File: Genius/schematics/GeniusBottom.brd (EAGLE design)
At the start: 50 x 100 mm, 160 parts, among them IC1 TL074D, IC10 USBLC6-2SC6, IC2 IS42S16400J, IC3 LM321MF, IC4 CS4271, IC5 OPA1678IDR, IC6 OPA1678IDR, IC7 MIC2005A-1YM6, IC8 STM32H743ZGTx, IC9 N25Q128A13, Q1 SI2309CDS, Q2 2N7002P, Q601 BC846, Q701 BC846, Q801 BC846, Q903 BC846, U4 TLV1117LV33, X1 53048-05, X4 FH12-24S-0.5SH, Y1 24.576MHz, Y2 25MHz

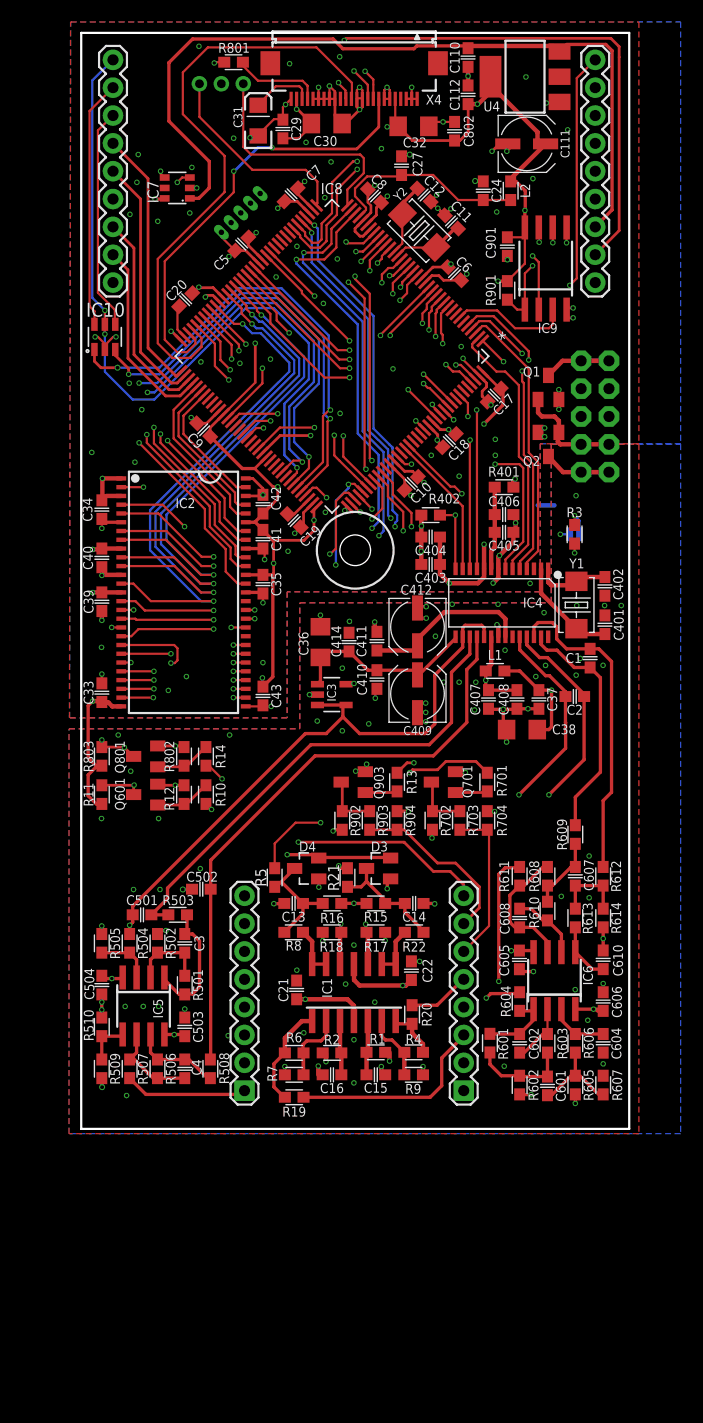
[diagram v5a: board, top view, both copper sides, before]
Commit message: Renumbered parts. Rev02.
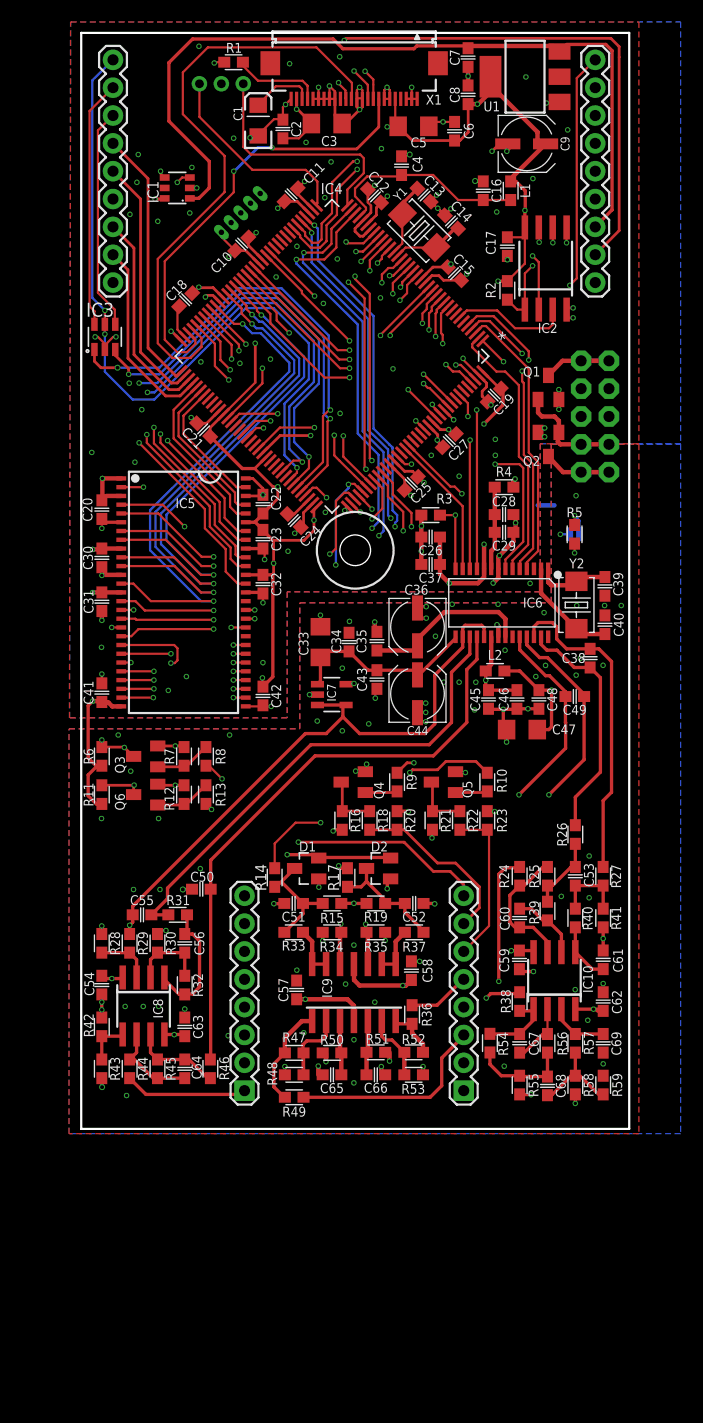
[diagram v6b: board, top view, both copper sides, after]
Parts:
- removed C110, C112, C405, C410, C411, C414, C802, C901: 100n, Rebel:C0603
- removed C111, C412: 47u, Rebel:CPOL-5
- removed C401, C402: 39p C0G, Rebel:C0603
- removed C403: 1u, Rebel:C0603
- removed R401: 5R1, Rebel:0603
- removed R402, R803, R901, R904: 10k, Rebel:0603
- removed R701: 1k, Rebel:0603
- removed R702, R902: 2k, Rebel:0603
- removed R703, R903: 100R, Rebel:0603
- removed R801: 560k, Rebel:0603
- removed R802: 1M, Rebel:0603
- removed X4: FH12-24S-0.5SH, con-hirose:FH12-24S-0.5SH
- added C23, C25, C48, C57, C58: 100n, Rebel:C0603
- added C47: 10u, Rebel:C1206
- added C49: 47n, Rebel:C0603
- added C51, C52, C65, C66: 10n C0G, Rebel:C0603
- added C56, C64: 100p C0G, Rebel:C0603
- added R33, R37, R50, R51: 2k, Rebel:0603
- added R34, R35: 100k, Rebel:0603
- added R36, R49: 100R, Rebel:0603
- added R47, R52: 20k, Rebel:0603
- added R48, R53: 10k, Rebel:0603
- added X100: 53048-05, con-molex:53048-05
- C1: value 47n -> 4u7 16V Tantalum; device Rebel:C0603 -> smartplug:EIA3216
- C11, C12: value 20p -> 100n
- C13, C14: value 10n C0G -> 20p
- C15, C16: value 10n C0G -> 100n
- C18: value 1u -> 4u7
- C19, C20: value 4u7 -> 100n
- C2: value 47n -> 100n
- C24: value 100n -> 4u7
- C27: value 10n -> 1u
- C3: value 100p C0G -> 10u; device Rebel:C0603 -> Rebel:C1206
- C30, C32: value 10u -> 100n; device Rebel:C1206 -> Rebel:C0603
- C31: value 4u7 16V Tantalum -> 100n; device smartplug:EIA3216 -> Rebel:C0603
- C33, C5: value 100n -> 10u; device Rebel:C0603 -> Rebel:C1206
- C36: value 10u -> 47u; device Rebel:C1206 -> Rebel:CPOL-5
- C37: value 100n -> 1u
- C38: value 10u -> 47n; device Rebel:C1206 -> Rebel:C0603
- C39, C40: value 100n -> 39p C0G
- C4: value 100p C0G -> 10n
- C9: value 100n -> 47u; device Rebel:C0603 -> Rebel:CPOL-5
- IC1: value TL074D -> MIC2005A-1YM6; device linear:SO14 -> James:SOT23-6
- IC10: value USBLC6-2SC6 -> OPA1678IDR; device usblc6:SOT-23-6L -> linear:SO08
- IC2: value IS42S16400J -> N25Q128A13; device James:TSOP54-400 -> Rebel:SO8W
- IC3: value LM321MF -> USBLC6-2SC6; device linear:SOT23-5 -> usblc6:SOT-23-6L
- IC4: value CS4271 -> STM32H743ZGTx; device Rebel:TSSOP28-0.65-9.7X4.4MM -> Rebel:QFP50P2200X2200X160-144N
- IC5: value OPA1678IDR -> IS42S16400J; device linear:SO08 -> James:TSOP54-400
- IC6: value OPA1678IDR -> CS4271; device linear:SO08 -> Rebel:TSSOP28-0.65-9.7X4.4MM
- IC7: value MIC2005A-1YM6 -> LM321MF; device James:SOT23-6 -> linear:SOT23-5
- IC8: value STM32H743ZGTx -> OPA1678IDR; device Rebel:QFP50P2200X2200X160-144N -> linear:SO08
- IC9: value N25Q128A13 -> TL074D; device Rebel:SO8W -> linear:SO14
- JP1: value (none) -> M09; device SparkFun:1X08 -> SparkFun:1X09
- JP4: value M09 -> (none); device SparkFun:1X09 -> SparkFun:1X08
- R1: value 2k -> 560k
- R10: value 100k -> 1k
- R13: value 1k -> 100k
- R14, R17, R18: value 100k -> 100R
- R16: value 1k -> 2k
- R19: value 100R -> 1k
- R2: value 2k -> 10k
- R20, R5: value 100R -> 10k
- R21: value 100R -> 2k
- R22: value 2k -> 100R
- R4: value 20k -> 5R1
- R6: value 20k -> 10k
- R7: value 10k -> 1M
- R8: value 2k -> 100k
- R9: value 10k -> 1k
- X1: value 53048-05 -> FH12-24S-0.5SH; device con-molex:53048-05 -> con-hirose:FH12-24S-0.5SH
- Y1: value 24.576MHz -> 25MHz
- Y2: value 25MHz -> 24.576MHz
- moved JP1 94.8 mm to (2.90, 97.5), turned to 270 degrees
- moved JP4 94.8 mm to (34.9, 3.49), turned to 90 degrees
- moved R1 91.3 mm to (13.9, 97.3), turned to 0 degrees
- moved C4 84.7 mm to (29.2, 87.9)
- moved C16 81.8 mm to (36.7, 85.6), turned to 90 degrees
- moved C3 75.9 mm to (22.4, 91.7), turned to 180 degrees
- moved IC1 75.2 mm to (8.76, 85.9), turned to 90 degrees
- moved C15 73.4 mm to (34.1, 78.0), turned to 315 degrees
- moved IC10 71.6 mm to (43.2, 13.5)
- moved R2 71.4 mm to (38.9, 76.5), turned to 270 degrees
- moved IC9 68.3 mm to (24.9, 12.4)
- moved C13 65.7 mm to (31.3, 85.2), turned to 315 degrees
- moved C14 62.3 mm to (33.8, 82.8), turned to 135 degrees
- moved IC8 61.7 mm to (5.69, 11.2), turned to 180 degrees
- moved C2 58.2 mm to (18.4, 91.2), turned to 270 degrees
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- renumbered C404 to C26, C406 to C28, C407 to C45, C408 to C46, C409 to C44, C501 to C55, C502 to C50, C503 to C63, C504 to C54, C601 to C68, C602 to C67, C604 to C69, C605 to C59, C606 to C62, C607 to C53, C608 to C60, C610 to C61, D3 to D2, D4 to D1, Q601 to Q6, Q701 to Q5, Q801 to Q3, Q903 to Q4, R501 to R32, R502 to R30, R503 to R31, R504 to R29, R505 to R28, R506 to R45, R507 to R44, R508 to R46, R509 to R43, R510 to R42, R601 to R54, R602 to R55, R603 to R56, R604 to R38, R605 to R58, R606 to R57, R607 to R59, R608 to R25, R609 to R26, R610 to R39, R611 to R24, R612 to R27, R613 to R40, R614 to R41, R704 to R23, U4 to U1
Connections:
- net +12V: now also C2.2, C3.2, C57.1, IC10.8, IC7.5, IC8.8, IC9.4, JP2.8, R16.1, R21.2, X1.23; no longer C21.1, C29.2, C30.2, IC1.4, IC3.5, IC5.8, IC6.8, JP4.8, R702.2, R902.1, X4.23
- net +3.3V: now also C11.1, C12.1, C15.1, C19.1, C20.1, C21.1, C22.1, C23.1, C25.1, C27.1, C30.1, C31.1, C32.1, C37.1, C5.2, C6.2, C9.+, IC2.8, IC4.108, IC4.121, IC4.131, IC4.144, IC4.17, IC4.30, IC4.32, IC4.39, IC4.52, IC4.62, IC4.72, IC4.84, IC4.95, IC5.1, IC5.14, IC5.27, IC5.3, IC5.43, IC5.49, IC5.9, IC6.10, L1.2, R2.1, R6.1, X1.5, X100.1; no longer C111.+, C112.1, C18.1, C32.2, C33.1, C34.1, C35.1, C39.1, C40.1, C403.1, C43.1, C5.1, C6.1, C7.1, C802.2, C9.1, C901.1, IC2.1, IC2.14, IC2.27, IC2.3, IC2.43, IC2.49, IC2.9, IC4.10, IC8.108, IC8.121, IC8.131, IC8.144, IC8.17, IC8.30, IC8.32, IC8.39, IC8.52, IC8.62, IC8.72, IC8.84, IC8.95, IC9.8, L2.2, R803.1, R901.1, X1.1, X4.5
- net +5V: now also C47.1, C48.1, C7.2, IC1.1, JP2.7, L2.1, R4.2; no longer C110.2, C37.1, C38.1, IC7.1, JP4.7, L1.1, R401.2
- net -12V: now also C58.1, IC10.4, IC7.2, IC8.4, IC9.11; no longer C22.1, IC1.11, IC3.2, IC5.4, IC6.4
- net ADC0: now also IC4.34, R14.2; no longer IC8.34, R5.2
- net ADC1: now also IC4.35, R17.2; no longer IC8.35, R21.2
- net AINA: now also IC6.17; no longer IC4.17
- net AINB: now also IC6.18; no longer IC4.18
- net ANALOG_OUTA: now also IC10.1; no longer IC6.1
- net ANALOG_OUTB: now also IC10.7; no longer IC6.7
- net AOUTA+: now also C49.1, IC6.25; no longer C2.1, IC4.25
- net AOUTA-: now also C49.2, IC6.24; no longer C2.2, IC4.24
- net AOUTB+: now also C38.2, IC6.26; no longer C1.2, IC4.26
- net AOUTB-: now also C38.1, IC6.27; no longer C1.1, IC4.27
- net BOOT: now also IC4.138, R5.2; no longer IC8.138, R3.2
- net CS_!CS: now also IC4.124, IC6.13; no longer IC4.13, IC8.124
- net CS_!RST: now also IC4.125, IC6.14, R3.2; no longer IC4.14, IC8.125, R402.2
- net CS_LRCK: now also IC4.3, IC6.4; no longer IC4.4, IC8.3
- net CS_SCK: now also IC4.1, IC6.11; no longer IC4.11, IC8.1
- net CS_SCLK: now also IC4.4, IC6.5; no longer IC4.5, IC8.4
- net CS_SDA: now also IC4.5, IC6.12; no longer IC4.12, IC8.5
- net CS_SDIN: now also IC4.122, IC6.7; no longer IC4.7, IC8.122
- net CS_SDOUT: now also IC4.2, IC6.6; no longer IC4.6, IC8.2
- net CS_VQ1: now also C33.2, C34.1, C43.1, IC6.15, IC7.1; no longer C36.2, C410.1, C414.1, IC3.1, IC4.15
- net CS_VREF: now also IC6.16, IC6.19, IC7.3, IC7.4; no longer IC3.3, IC3.4, IC4.16, IC4.19
- net CVINA: now also IC9.12, JP3.5, R34.2; no longer IC1.12, JP1.5, R18.2
- net CVINB: now also IC9.10, JP3.3, R35.2; no longer IC1.10, JP1.3, R17.2
- net CVOUTA: now also JP4.5, R36.2; no longer JP3.5, R20.2
- net CVOUTB: now also JP4.3, R49.2; no longer JP3.3, R19.2
- net DAC1: now also IC4.40, R51.1; no longer IC8.40, R1.1
- net DAC2: now also IC4.41, R50.1; no longer IC8.41, R2.1
- net DRAM_!CAS: now also IC4.132, IC5.17; no longer IC2.17, IC8.132
- net DRAM_!CS: now also IC4.136, IC5.19; no longer IC2.19, IC8.136
- net DRAM_!RAS: now also IC4.49, IC5.18; no longer IC2.18, IC8.49
- net DRAM_!WE: now also IC4.26, IC5.16; no longer IC2.16, IC8.26
- net DRAM_A0: now also IC4.10, IC5.23; no longer IC2.23, IC8.10
- net DRAM_A1: now also IC4.11, IC5.24; no longer IC2.24, IC8.11
- net DRAM_A10: now also IC4.56, IC5.22; no longer IC2.22, IC8.56
- net DRAM_A11: now also IC4.57, IC5.35; no longer IC2.35, IC8.57
- net DRAM_A2: now also IC4.12, IC5.25; no longer IC2.25, IC8.12
- net DRAM_A3: now also IC4.13, IC5.26; no longer IC2.26, IC8.13
- net DRAM_A4: now also IC4.14, IC5.29; no longer IC2.29, IC8.14
- net DRAM_A5: now also IC4.15, IC5.30; no longer IC2.30, IC8.15
- net DRAM_A6: now also IC4.50, IC5.31; no longer IC2.31, IC8.50
- net DRAM_A7: now also IC4.53, IC5.32; no longer IC2.32, IC8.53
- net DRAM_A8: now also IC4.54, IC5.33; no longer IC2.33, IC8.54
- net DRAM_A9: now also IC4.55, IC5.34; no longer IC2.34, IC8.55
- net DRAM_BA0: now also IC4.89, IC5.20; no longer IC2.20, IC8.89
- net DRAM_BA1: now also IC4.90, IC5.21; no longer IC2.21, IC8.90
- net DRAM_CKE: now also IC4.135, IC5.37; no longer IC2.37, IC8.135
- net DRAM_CLK: now also IC4.93, IC5.38; no longer IC2.38, IC8.93
- net DRAM_DQ0: now also IC4.85, IC5.2; no longer IC2.2, IC8.85
- net DRAM_DQ1: now also IC4.86, IC5.4; no longer IC2.4, IC8.86
- net DRAM_DQ10: now also IC4.66, IC5.45; no longer IC2.45, IC8.66
- net DRAM_DQ11: now also IC4.67, IC5.47; no longer IC2.47, IC8.67
- net DRAM_DQ12: now also IC4.68, IC5.48; no longer IC2.48, IC8.68
- net DRAM_DQ13: now also IC4.77, IC5.50; no longer IC2.50, IC8.77
- net DRAM_DQ14: now also IC4.78, IC5.51; no longer IC2.51, IC8.78
- net DRAM_DQ15: now also IC4.79, IC5.53; no longer IC2.53, IC8.79
- net DRAM_DQ2: now also IC4.114, IC5.5; no longer IC2.5, IC8.114
- net DRAM_DQ3: now also IC4.115, IC5.7; no longer IC2.7, IC8.115
- net DRAM_DQ4: now also IC4.58, IC5.8; no longer IC2.8, IC8.58
- net DRAM_DQ5: now also IC4.59, IC5.10; no longer IC2.10, IC8.59
- net DRAM_DQ6: now also IC4.60, IC5.11; no longer IC2.11, IC8.60
- net DRAM_DQ7: now also IC4.63, IC5.13; no longer IC2.13, IC8.63
- net DRAM_DQ8: now also IC4.64, IC5.42; no longer IC2.42, IC8.64
- net DRAM_DQ9: now also IC4.65, IC5.44; no longer IC2.44, IC8.65
- net DRAM_LDQM: now also IC4.141, IC5.15; no longer IC2.15, IC8.141
- net DRAM_UDQM: now also IC4.142, IC5.39; no longer IC2.39, IC8.142
- net ENC1_A: now also IC4.42, JP2.2; no longer IC8.42, JP4.2
- net ENC1_B: now also IC4.43, JP2.3; no longer IC8.43, JP4.3
- net ENC1_SW: now also IC4.129, JP2.1; no longer IC8.129, JP4.1
- net ENC2_A: now also IC4.110, JP2.5; no longer IC8.110, JP4.5
- net ENC2_B: now also IC4.133, JP2.6; no longer IC8.133, JP4.6
- net ENC2_SW: now also IC4.134, JP2.4; no longer IC8.134, JP4.4
- net FLASH_CLK: now also IC2.6, IC4.19; no longer IC8.19, IC9.6
- net FLASH_HOLD: now also IC2.7, IC4.22; no longer IC8.22, IC9.7
- net FLASH_MISO: now also IC2.2, IC4.20; no longer IC8.20, IC9.2
- net FLASH_MOSI: now also IC2.5, IC4.21; no longer IC8.21, IC9.5
- net FLASH_NCS: now also IC2.1, IC4.18, R2.2; no longer IC8.18, IC9.1, R901.2
- net FLASH_W: now also IC2.3, IC4.7; no longer IC8.7, IC9.3
- net GND: now also C1.C, C2.1, C23.2, C25.2, C29.2, C3.1, C30.2, C31.2, C32.2, C33.1, C36.-, C4.2, C47.2, C48.2, C5.1, C51.2, C52.2, C57.2, C58.2, C6.1, C65.2, C66.2, C7.1, C9.-, IC1.2, IC2.4, IC3.2, IC4.107, IC4.120, IC4.130, IC4.143, IC4.16, IC4.31, IC4.38, IC4.51, IC4.61, IC4.83, IC4.94, IC5.12, IC5.28, IC5.41, IC5.46, IC5.52, IC5.54, IC5.6, IC6.21, IC6.8, JP1.9, JP4.4, R1.1, R19.2, R20.1, R34.1, R35.1, R48.1, R5.1, R53.1, R7.2, X1.1, X1.11, X1.12, X1.16, X1.17, X1.18, X1.19, X1.2, X1.20, X1.24, X1.6, X1.7, X100.3; no longer C110.1, C111.-, C112.2, C29.1, C30.1, C31.C, C32.1, C33.2, C36.1, C38.2, C401.2, C402.2, C403.2, C405.2, C410.2, C411.2, C412.-, C414.2, C5.2, C6.2, C7.2, C802.1, C9.2, C901.2, IC10.2, IC2.12, IC2.28, IC2.41, IC2.46, IC2.52, IC2.54, IC2.6, IC4.21, IC4.8, IC7.2, IC8.107, IC8.120, IC8.130, IC8.143, IC8.16, IC8.31, IC8.38, IC8.51, IC8.61, IC8.83, IC8.94, IC9.4, JP1.4, JP4.9, R16.2, R17.1, R18.1, R402.1, R7.1, R801.1, R802.2, R9.1, R904.1, X4.1, X4.11, X4.12, X4.16, X4.17, X4.18, X4.19, X4.2, X4.20, X4.24, X4.3, X4.6, X4.7
- net INL: now also JP3.2; no longer JP1.2
- net INR: now also JP3.1; no longer JP1.1
- net N$11: now also C13.1, IC4.24, Y1.1; no longer C12.1, IC8.24, Y2.1
- net N$12: now also IC9.2, R47.1, R48.2; no longer IC1.2, R6.1, R7.2
- net N$13: now also IC10.2; no longer IC6.2
- net N$14: now also IC10.3; no longer IC6.3
- net N$15: now also IC9.6, R52.1, R53.2; no longer IC1.6, R4.1, R9.2
- net N$17: now also C14.1, IC4.23, Y1.2; no longer C11.1, IC8.23, Y2.2
- net N$18: now also C39.1, IC6.1, Y2.1; no longer C402.1, IC4.1, Y1.1
- net N$19: now also IC3.6, JP1.2; no longer IC10.6, JP2.2
- net N$2: now also C51.1, R14.1, R15.1, R33.2; no longer C13.1, R16.1, R5.1, R8.2
- net N$20: now also C35.1, C36.+, IC6.22; no longer C411.1, C412.+, IC4.22
- net N$21: now also C40.1, IC6.2, Y2.2; no longer C401.1, IC4.2, Y1.2
- net N$22: now also C52.1, R17.1, R19.1, R37.2; no longer C14.1, R15.1, R21.1, R22.2
- net N$27: now also IC10.6; no longer IC6.6
- net N$28: now also IC10.5; no longer IC6.5
- net N$3: now also IC6.20, L2.2; no longer IC4.20, L1.2
- net N$30: now also IC9.13, IC9.14, R33.1; no longer IC1.13, IC1.14, R8.1
- net N$31: now also C65.1, IC9.3, R50.2; no longer C16.1, IC1.3, R2.2
- net N$32: now also IC9.1, R47.2, R49.1; no longer IC1.1, R19.1, R6.2
- net N$33: now also C24.1, IC4.106; no longer C19.1, IC8.106
- net N$34: now also C18.1, IC4.71; no longer C20.1, IC8.71
- net N$36: now also IC8.3; no longer IC5.3
- net N$37: now also R13.2; no longer R10.2
- net N$38: now also C56.1, IC8.2; no longer C3.1, IC5.2
- net N$39: now also R10.1; no longer R701.1
- net N$4: now also IC9.7, R36.1, R52.2; no longer IC1.7, R20.1, R4.2
- net N$40: now also C56.2, IC8.1; no longer C3.2, IC5.1
- net N$41: now also R21.1, R22.1; no longer R702.1, R703.1
- net N$42: now also IC8.5; no longer IC5.5
- net N$43: now also C64.1, IC8.6; no longer C4.1, IC5.6
- net N$44: now also C66.1, IC9.5, R51.2; no longer C15.1, IC1.5, R1.2
- net N$45: now also C64.2, IC8.7; no longer C4.2, IC5.7
- net N$46: now also IC4.48; no longer IC8.48
- net N$47: now also R9.1; no longer R13.1
- net N$48: now also IC4.100; no longer IC8.100
- net N$5: now also IC9.8, IC9.9, R37.1; no longer IC1.8, IC1.9, R22.1
- net N$51: now also R16.2, R18.1; no longer R902.2, R903.1
- net N$54: now also R7.1, R8.2; no longer R14.2, R802.1
- net N$55: now also IC3.4, JP1.3; no longer IC10.4, JP2.3
- net N$6: now also C1.A, X1.22; no longer C31.A, X4.22
- net N$8: now also R1.2, X1.21; no longer R801.2, X4.21
- net NRST: now also IC4.25, X100.5; no longer IC8.25, X1.5
- net OLED_CS: now also IC4.70, X1.8; no longer IC8.70, X4.8
- net OLED_DC: now also IC4.29, X1.10; no longer IC8.29, X4.10
- net OLED_MOSI: now also IC4.27, X1.14; no longer IC8.27, X4.14
- net OLED_RST: now also IC4.28, X1.9; no longer IC8.28, X4.9
- net OLED_SCK: now also IC4.69, X1.13; no longer IC8.69, X4.13
- net OUTL: now also JP4.2; no longer JP3.2
- net OUTR: now also JP4.1; no longer JP3.1
- net SWCLK: now also IC4.109, X100.2; no longer IC8.109, X1.2
- net SWDIO: now also IC4.105, X100.4; no longer IC8.105, X1.4
- net SW_A: now also IC4.111, JP3.8; no longer IC8.111, JP1.8
- net SW_B: now also IC4.113, JP4.8; no longer IC8.113, JP3.8
- net TRINA: now also JP3.7, R8.1; no longer JP1.7, R14.1
- net TRINB: now also JP3.6, R13.1; no longer JP1.6, R10.1
- net TROUTA: now also JP4.7, R18.2, R20.2; no longer JP3.7, R903.2, R904.2
- net TROUTB: now also JP4.6, R22.2; no longer JP3.6, R703.2
- net TR_IN_A: now also IC4.112, R6.2; no longer IC8.112, R803.2
- net TR_IN_B: now also IC4.116; no longer IC8.116
- net TR_OUT_A: now also IC4.118, R9.2; no longer IC8.118, R13.2
- net TR_OUT_B: now also IC4.117, R10.2; no longer IC8.117, R701.2
- net UART5_RX: now also IC4.73, JP1.4; no longer IC8.73, JP2.4
- net UART5_TX: now also IC4.74, JP1.5; no longer IC8.74, JP2.5
- net UART_MCU_RX: now also IC4.37; no longer IC8.37
- net UART_MCU_TX: now also IC4.36; no longer IC8.36
- net USBD_DM: now also IC3.1, IC4.103; no longer IC10.1, IC8.103
- net USBD_DP: now also IC3.3, IC4.104; no longer IC10.3, IC8.104
- net USBD_VBUS: now also IC3.5, IC4.101, JP1.1; no longer IC10.5, IC8.101, JP2.1
- net USBH_DM: now also IC4.75, JP1.7; no longer IC8.75, JP2.7
- net USBH_DP: now also IC4.76, JP1.8; no longer IC8.76, JP2.8
- net USBH_PWR_EN: now also IC1.3, IC4.99; no longer IC7.3, IC8.99
- net USBH_PWR_FAULT: now also IC1.4, IC4.102; no longer IC7.4, IC8.102
- net USBH_VBUS: now also IC1.6, JP1.6; no longer IC7.6, JP2.6
- net VD: now also C29.1, IC6.9, R4.1; no longer C405.1, IC4.9, R401.1
- net VDDA: now also C16.1, C4.1, IC4.33, L1.1; no longer C24.1, C27.1, IC8.33, L2.1
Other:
- board text added: "Genius Rev02"
- board text removed: "Genius Rev01"

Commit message: added I2C bus
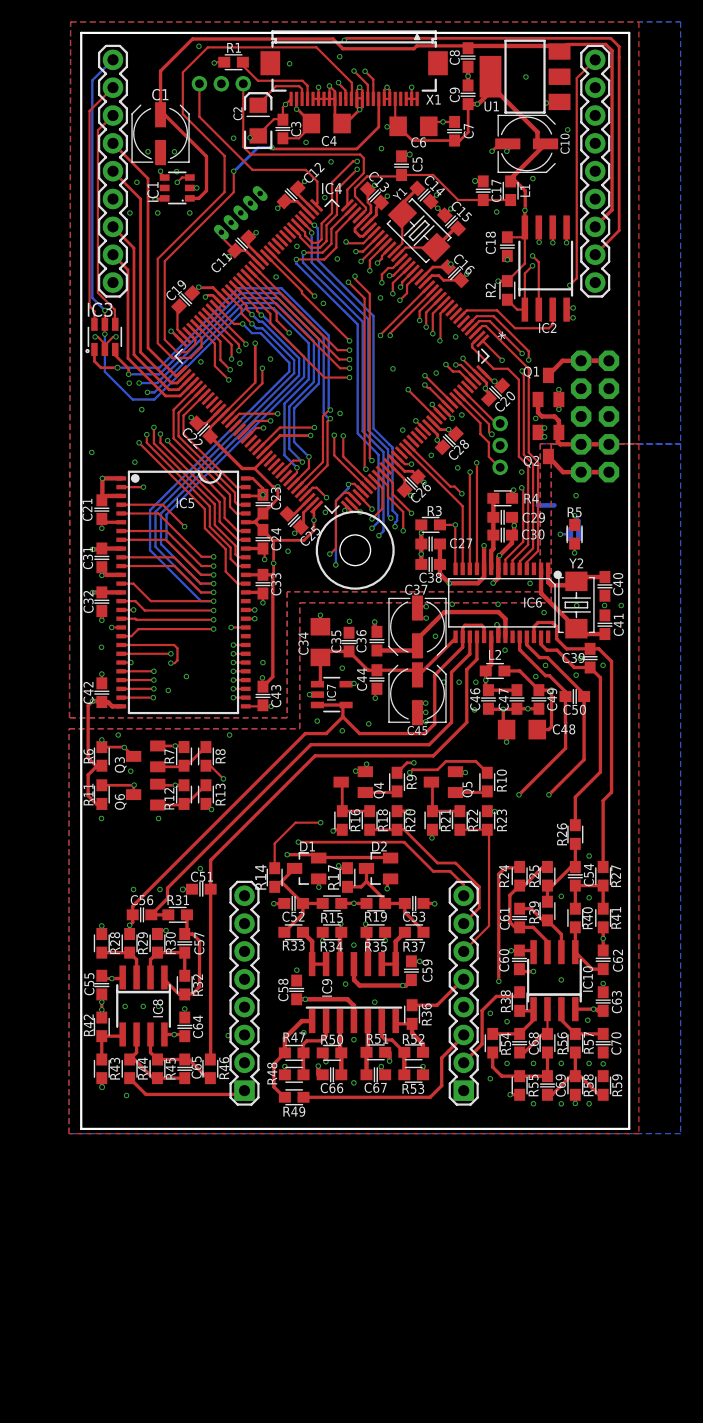
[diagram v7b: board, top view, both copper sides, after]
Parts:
- added C70: 100p C0G, Rebel:C0603
- added I2C: (no value), Rebel:JST-B3B-PH-KL
- C1: value 4u7 16V Tantalum -> 47u; device smartplug:EIA3216 -> Rebel:CPOL-5
- C10: value 100n -> 47u; device Rebel:C0603 -> Rebel:CPOL-5
- C13: value 20p -> 100n
- C15: value 100n -> 20p
- C18, C24: value 4u7 -> 100n
- C19, C25: value 100n -> 4u7
- C2: value 100n -> 4u7 16V Tantalum; device Rebel:C0603 -> smartplug:EIA3216
- C27: value 1u -> 100n
- C29, C46: value 100n -> 1u
- C3, C33, C47: value 10u -> 100n; device Rebel:C1206 -> Rebel:C0603
- C34, C48, C6: value 100n -> 10u; device Rebel:C0603 -> Rebel:C1206
- C36, C9: value 47u -> 100n; device Rebel:CPOL-5 -> Rebel:C0603
- C37: value 1u -> 47u; device Rebel:C0603 -> Rebel:CPOL-5
- C38: value 47n -> 1u
- C39: value 39p C0G -> 47n
- C4: value 10n -> 10u; device Rebel:C0603 -> Rebel:C1206
- C41: value 100n -> 39p C0G
- C44: value 10u -> 100n; device Rebel:CPOL-5 -> Rebel:C0603
- C45: value 1u -> 10u; device Rebel:C0603 -> Rebel:CPOL-5
- C49: value 47n -> 100n
- C5: value 10u -> 10n; device Rebel:C1206 -> Rebel:C0603
- C50: value 2n7 C0G -> 47n
- C51: value 10n C0G -> 2n7 C0G
- C53: value 480p C0G -> 10n C0G
- C54: value 100n -> 480p C0G
- C55: value 2n7 C0G -> 100n
- C56: value 100p C0G -> 2n7 C0G
- C57, C62: value 100n -> 100p C0G
- C60, C64: value 100p C0G -> 100n
- C65: value 10n C0G -> 100p C0G
- C67: value 100p C0G -> 10n C0G
- C68: value 480p C0G -> 100p C0G
- C69: value 100p C0G -> 480p C0G
- R10, R9: value 1k -> 10k
- moved C41 46.3 mm to (47.8, 46.0)
- moved C54 44.3 mm to (45.1, 23.0), turned to 90 degrees
- moved C50 38.3 mm to (45.0, 39.5)
- moved C63 38.2 mm to (47.6, 11.6)
- moved C20 37.5 mm to (37.8, 67.2), turned to 225 degrees
- moved C30 36.6 mm to (38.5, 54.2), turned to 0 degrees
- moved C18 29.7 mm to (38.9, 80.5), turned to 270 degrees
- moved C19 29.5 mm to (9.53, 75.7), turned to 45 degrees
- moved C10 27.6 mm to (40.6, 89.9), turned to 0 degrees
- moved C38 16.9 mm to (31.9, 51.5), turned to 180 degrees
- moved C53 14.9 mm to (30.4, 20.6), turned to 0 degrees
- moved C32 14.8 mm to (1.88, 48.1)
- moved C42 14.7 mm to (1.88, 39.8), turned to 90 degrees
- moved C65 13.4 mm to (9.45, 5.48), turned to 90 degrees
- moved C67 13.4 mm to (26.9, 4.93), turned to 0 degrees
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- renumbered X100 to X2
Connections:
- new net I2C_SCL: I2C.1, IC4.139
- new net I2C_SDA: I2C.3, IC4.137
- net +12V: now also C4.2, C58.1, C60.1, C64.1; no longer C2.2, C57.1, C59.1, C63.1
- net +3.3V: now also C10.+, C13.1, C16.1, C18.1, C24.1, C28.1, C33.1, C38.1, C43.1, C7.2, C9.1; no longer C10.1, C15.1, C17.1, C19.1, C25.1, C30.1, C37.1, C41.1, C5.2, C8.1, C9.+
- net +5V: now also C1.+, C49.1, C8.2; no longer C47.1, C7.2
- net -12V: now also C55.1, C59.1, C63.1; no longer C54.1, C58.1, C62.1
- net AINA: now also C56.1; no longer C55.1
- net AINB: now also C51.1; no longer C50.1
- net ANALOG_OUTA: now also C68.2; no longer C67.2
- net ANALOG_OUTB: now also C61.2; no longer C60.2
- net AOUTA+: now also C50.1; no longer C49.1
- net AOUTA-: now also C50.2; no longer C49.2
- net AOUTB+: now also C39.2; no longer C38.2
- net AOUTB-: now also C39.1; no longer C38.1
- net CS_VQ1: now also C34.2, C35.1, C44.1, C45.+; no longer C33.2, C34.1, C43.1, C44.+
- net CS_VREF: now also C51.2, C56.2; no longer C50.2, C55.2
- net GND: now also C1.-, C10.-, C2.C, C33.2, C34.1, C36.2, C37.-, C38.2, C4.1, C44.2, C45.-, C49.2, C5.2, C53.2, C55.2, C60.2, C64.2, C67.2, C70.2, C8.1, C9.2, I2C.2; no longer C1.C, C10.2, C2.1, C33.1, C34.2, C36.-, C37.2, C39.2, C4.2, C44.-, C45.2, C5.1, C51.2, C54.2, C57.2, C61.2, C65.2, C69.2, C8.2, C9.-
- net N$1: now also C69.1; no longer C68.1
- net N$10: now also C69.2; no longer C68.2
- net N$11: now also C14.1; no longer C13.1
- net N$13: now also C68.1; no longer C67.1
- net N$14: now also C70.1; no longer C69.1
- net N$17: now also C15.1; no longer C14.1
- net N$18: now also C40.1; no longer C39.1
- net N$2: now also C52.1; no longer C51.1
- net N$20: now also C36.1, C37.+; no longer C35.1, C36.+
- net N$21: now also C41.1; no longer C40.1
- net N$22: now also C53.1; no longer C52.1
- net N$25: now also C54.1; no longer C53.1
- net N$26: now also C54.2; no longer C53.2
- net N$27: now also C61.1; no longer C60.1
- net N$28: now also C62.1; no longer C61.1
- net N$3: now also C47.1; no longer C45.1
- net N$31: now also C66.1; no longer C65.1
- net N$33: now also C25.1; no longer C24.1
- net N$34: now also C19.1; no longer C18.1
- net N$38: now also C57.1; no longer C56.1
- net N$40: now also C57.2; no longer C56.2
- net N$43: now also C65.1; no longer C64.1
- net N$44: now also C67.1; no longer C66.1
- net N$45: now also C65.2; no longer C64.2
- net N$6: now also C2.A; no longer C1.A
- net VD: now also C30.1; no longer C28.1
- net VDDA: now also C17.1, C5.1; no longer C16.1, C4.1
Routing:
- net I2C_SDA: track 0.00 -> 8.00 mm
- net +3.3V: track 335.5 -> 328.0 mm
- net I2C_SCL: track 0.00 -> 4.58 mm
- net GND: track 180.7 -> 178.4 mm, vias 182 -> 196
- net BOOT: track 22.9 -> 21.7 mm
- net VD: track 7.58 -> 6.52 mm
- net CS_SDIN: track 21.8 -> 20.7 mm
- net +5V: track 139.5 -> 140.5 mm
- net DRAM_A0: track 55.4 -> 54.8 mm
- net DRAM_A3: track 58.4 -> 57.8 mm
- net DRAM_A1: track 56.4 -> 55.9 mm
- net DRAM_A2: track 57.4 -> 56.9 mm
- net OUTL: track 10.0 -> 9.57 mm, vias 1 -> 0

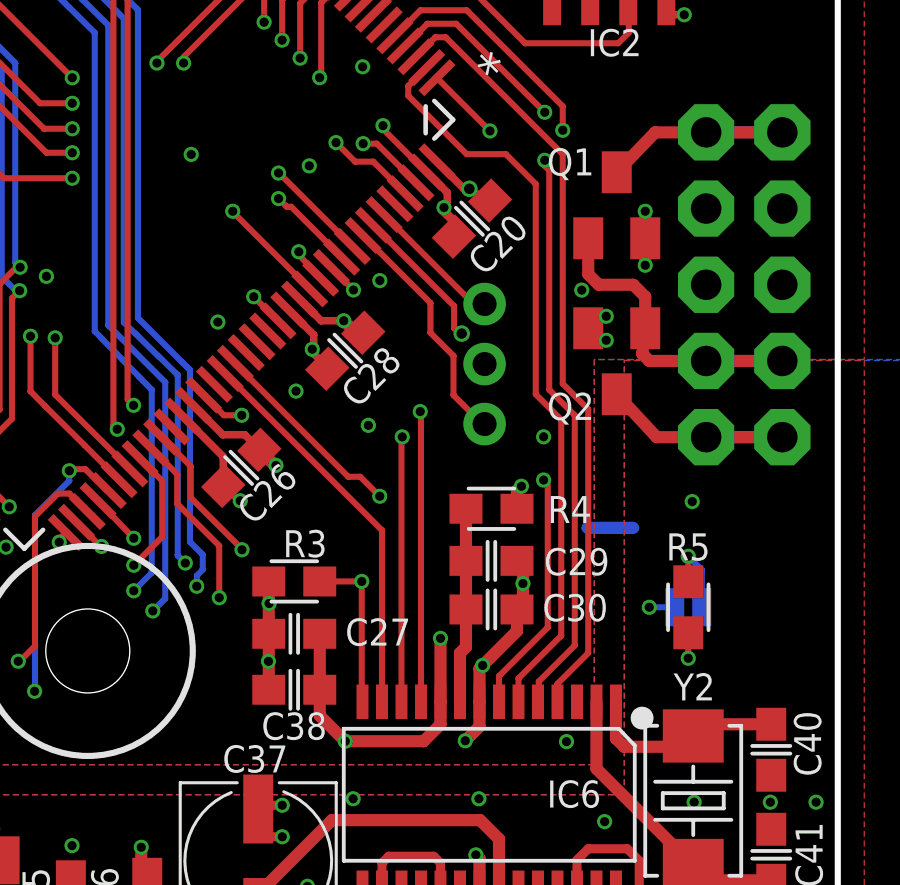
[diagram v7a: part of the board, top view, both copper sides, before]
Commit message: changed I2C to TT style pin header
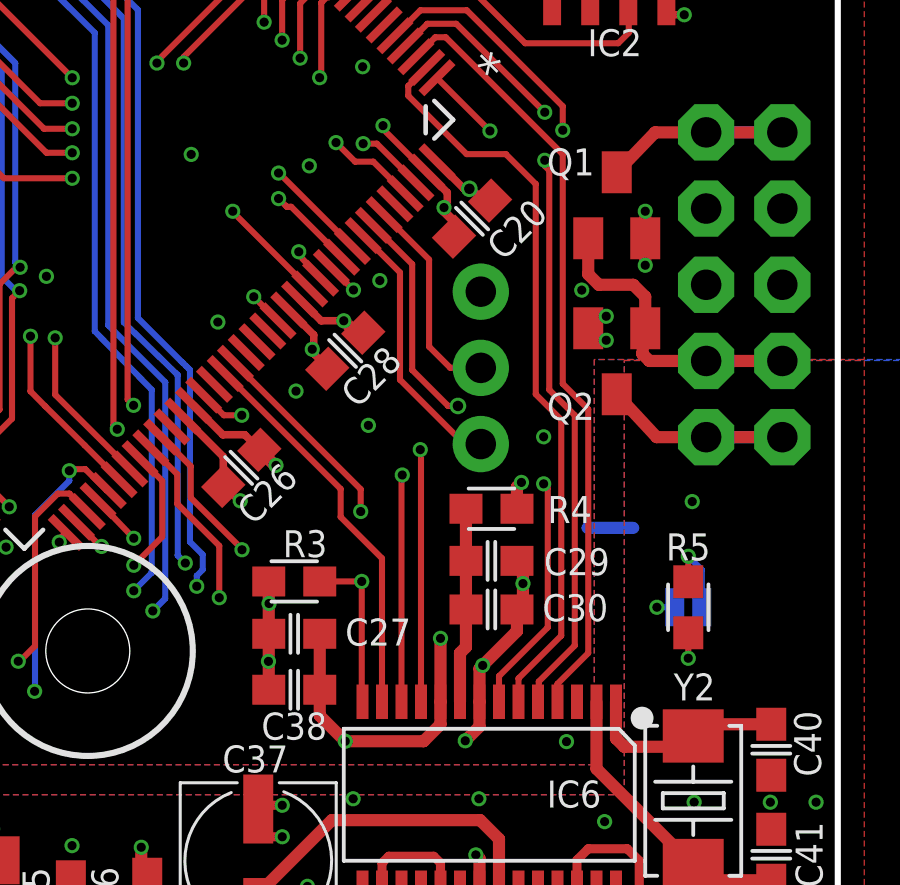
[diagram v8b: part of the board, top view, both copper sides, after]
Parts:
- I2C: device Rebel:JST-B3B-PH-KL -> SparkFun:1X03
- moved I2C 2.42 mm to (38.1, 64.8), turned to 270 degrees
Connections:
- net GND: now also I2C.1; no longer I2C.2
- net I2C_SCL: now also I2C.2; no longer I2C.1
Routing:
- net I2C_SCL: track 4.58 -> 7.04 mm
- net I2C_SDA: track 8.00 -> 8.89 mm
- net CS_!RST: track 15.2 -> 14.5 mm
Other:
- board text added: "GND"
- board text added: "SCL"
- board text added: "SDA"
